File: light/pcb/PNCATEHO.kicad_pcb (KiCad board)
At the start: 2 copper layers, 85.6 x 54 mm, 49 parts, among them J1 USB_C_Receptacle_USB2.0, U1 RP2040, U2 RT9013-33GB, U3 W25Q32JVSSIQ, Y1 12MHz

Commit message: fix footprint
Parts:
- SW1, SW10, SW2, SW3, SW4, SW5, SW6, SW7, SW8, SW9: footprint switches:SW_PG1316 -> PNCATEHO:SW_PG1316
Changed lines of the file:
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@@
 		(embedded_fonts no)
 	)
-	(footprint "switches:SW_PG1316"
+	(footprint "PNCATEHO:SW_PG1316"
 		(layer "F.Cu")
 		(at 107.08 86.253958)
@@
 		)
 		(embedded_fonts no)
-		(model "/home/miwayho/kicad/inpulib/step/switches/PG1316S.STEP"
+		(model "${KIPRJMOD}/lib/step/PG1316S.STEP"
 			(offset
 				(xyz -4.75 -6.25 -10.25)
@@
 		)
 	)
-	(footprint "switches:SW_PG1316"
+	(footprint "PNCATEHO:SW_PG1316"
 		(layer "F.Cu")
 		(at 157.93 86.253958)
@@
 		)
 		(embedded_fonts no)
-		(model "/home/miwayho/kicad/inpulib/step/switches/PG1316S.STEP"
+		(model "${KIPRJMOD}/lib/step/PG1316S.STEP"
 			(offset
 				(xyz -4.75 -6.25 -10.25)
@@
 		)
 	)
-	(footprint "switches:SW_PG1316"
+	(footprint "PNCATEHO:SW_PG1316"
 		(layer "F.Cu")
 		(at 157.93 120.153958)
@@
 		)
 		(embedded_fonts no)
-		(model "/home/miwayho/kicad/inpulib/step/switches/PG1316S.STEP"
+		(model "${KIPRJMOD}/lib/step/PG1316S.STEP"
 			(offset
 				(xyz -4.75 -6.25 -10.25)
@@
 		)
 	)
-	(footprint "switches:SW_PG1316"
+	(footprint "PNCATEHO:SW_PG1316"
 		(layer "F.Cu")
 		(at 124.03 86.253958)
@@
 		)
 		(embedded_fonts no)
-		(model "/home/miwayho/kicad/inpulib/step/switches/PG1316S.STEP"
+		(model "${KIPRJMOD}/lib/step/PG1316S.STEP"
 			(offset
 				(xyz -4.75 -6.25 -10.25)
@@
 		)
 	)
-	(footprint "switches:SW_PG1316"
+	(footprint "PNCATEHO:SW_PG1316"
 		(layer "F.Cu")
 		(at 107.08 103.203958)
@@
 		)
 		(embedded_fonts no)
-		(model "/home/miwayho/kicad/inpulib/step/switches/PG1316S.STEP"
+		(model "${KIPRJMOD}/lib/step/PG1316S.STEP"
 			(offset
 				(xyz -4.75 -6.25 -10.25)
@@
 		)
 	)
-	(footprint "switches:SW_PG1316"
+	(footprint "PNCATEHO:SW_PG1316"
 		(layer "F.Cu")
 		(at 140.98 103.203958)
@@
 		)
 		(embedded_fonts no)
-		(model "/home/miwayho/kicad/inpulib/step/switches/PG1316S.STEP"
+		(model "${KIPRJMOD}/lib/step/PG1316S.STEP"
 			(offset
 				(xyz -4.75 -6.25 -10.25)
@@
 		)
 	)
-	(footprint "switches:SW_PG1316"
+	(footprint "PNCATEHO:SW_PG1316"
 		(layer "F.Cu")
 		(at 157.93 103.203958)
@@
 		)
 		(embedded_fonts no)
-		(model "/home/miwayho/kicad/inpulib/step/switches/PG1316S.STEP"
+		(model "${KIPRJMOD}/lib/step/PG1316S.STEP"
 			(offset
 				(xyz -4.75 -6.25 -10.25)
@@
 		)
 	)
-	(footprint "switches:SW_PG1316"
+	(footprint "PNCATEHO:SW_PG1316"
 		(layer "F.Cu")
 		(at 174.88 120.153958)
@@
 		)
 		(embedded_fonts no)
-		(model "/home/miwayho/kicad/inpulib/step/switches/PG1316S.STEP"
+		(model "${KIPRJMOD}/lib/step/PG1316S.STEP"
 			(offset
 				(xyz -4.75 -6.25 -10.25)
@@
 		)
 	)
-	(footprint "switches:SW_PG1316"
+	(footprint "PNCATEHO:SW_PG1316"
 		(layer "F.Cu")
 		(at 140.98 86.253958)
@@
 		)
 		(embedded_fonts no)
-		(model "/home/miwayho/kicad/inpulib/step/switches/PG1316S.STEP"
+		(model "${KIPRJMOD}/lib/step/PG1316S.STEP"
 			(offset
 				(xyz -4.75 -6.25 -10.25)
@@
 		)
 	)
-	(footprint "switches:SW_PG1316"
+	(footprint "PNCATEHO:SW_PG1316"
 		(layer "F.Cu")
 		(at 124.03 103.203958)
@@
 		)
 		(embedded_fonts no)
-		(model "/home/miwayho/kicad/inpulib/step/switches/PG1316S.STEP"
+		(model "${KIPRJMOD}/lib/step/PG1316S.STEP"
 			(offset
 				(xyz -4.75 -6.25 -10.25)

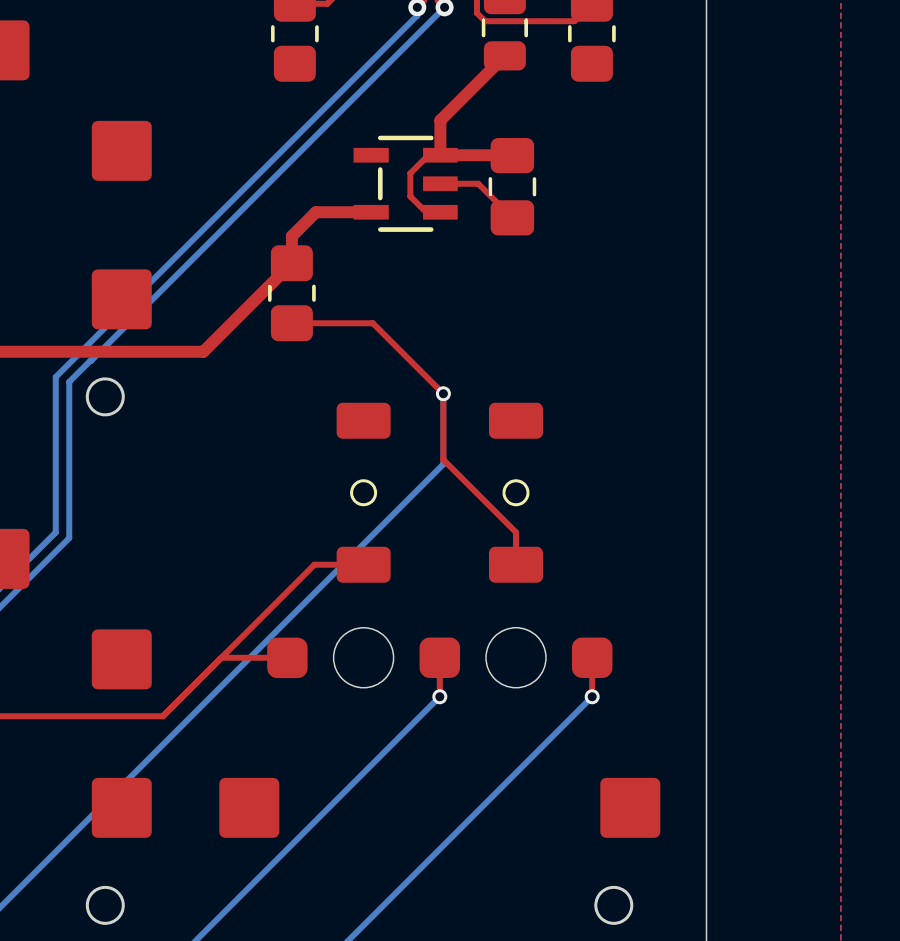
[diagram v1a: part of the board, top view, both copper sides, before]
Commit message: update outline
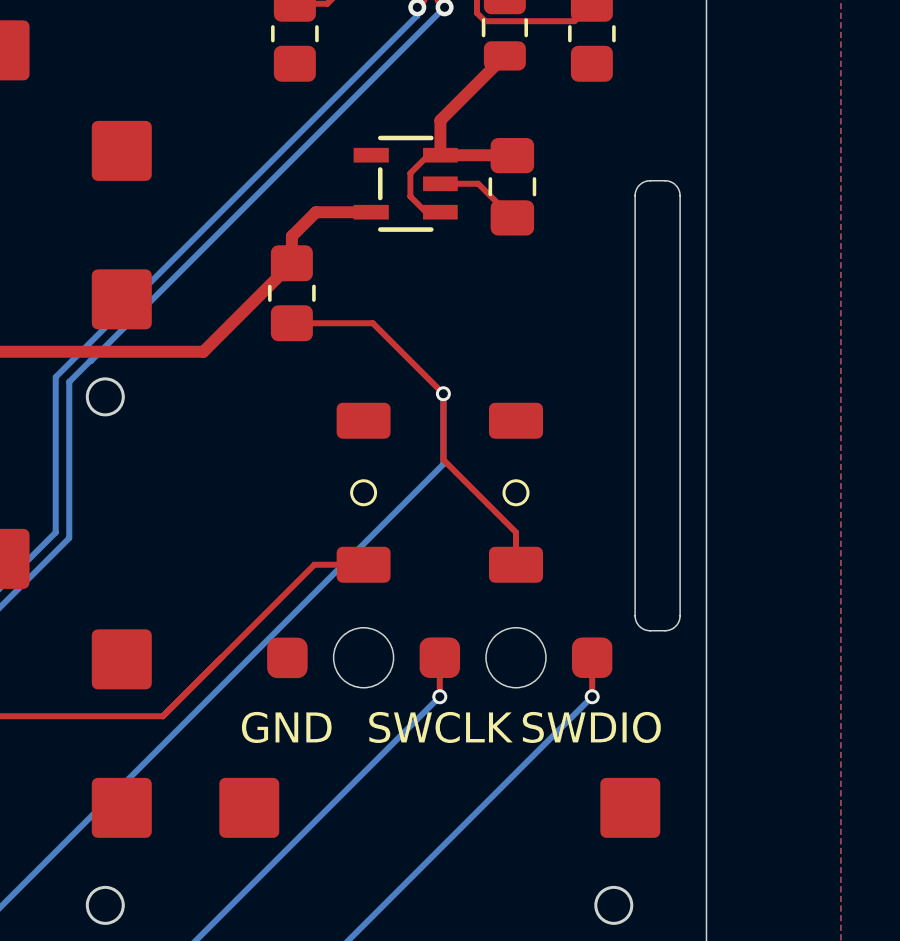
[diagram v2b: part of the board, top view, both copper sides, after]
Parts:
- SW1, SW10, SW2, SW3, SW4, SW5, SW6, SW7, SW8, SW9: footprint PNCATEHO:SW_PG1316 -> switches:SW_PG1316
- TP1: value Boot -> GND
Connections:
- TP1 pad 1: BOOT -> GND
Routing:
- net BOOT: track 46.7 -> 43.9 mm
- net GND: track 32.4 -> 33.0 mm
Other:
- outline, holes or cut-outs redrawn

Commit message: Some little fixes
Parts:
- SW1, SW10, SW2, SW3, SW4, SW5, SW6, SW7, SW8, SW9: footprint switches:SW_PG1316 -> PNCATEHO:SW_PG1316
- SW11: value ~ -> Boot
- SW12: value ~ -> Reset
- moved SW11 3.65 mm to (172.5, 100.0)
- moved SW12 3.65 mm to (177.3, 100.0)
- moved C7 2.00 mm to (116.8, 114.5)
- moved TP1 1.90 mm to (171.4, 108.2)
- moved TP2 1.90 mm to (178.3, 108.2)
- moved TP3 1.00 mm to (174.9, 108.2)
- moved R8 0.81 mm to (169.2, 97.1)
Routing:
- net +3V3: track 192.4 -> 189.9 mm
- net ~{RESET}: track 85.1 -> 83.1 mm
- net SWCLK: track 71.7 -> 72.7 mm
- net SWDIO: track 76.9 -> 76.2 mm
- net GND: track 33.0 -> 32.4 mm
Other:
- outline, holes or cut-outs redrawn
